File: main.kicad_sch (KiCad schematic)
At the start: 30 parts, among them J1 USB_C_Receptacle_USB2.0_16P, J2 Conn_ARM_JTAG_SWD_10, U1 XC6206PxxxMR, U2 USBLC6-2SC6, U3 CH340N, U4 E73-2G4M04S1B

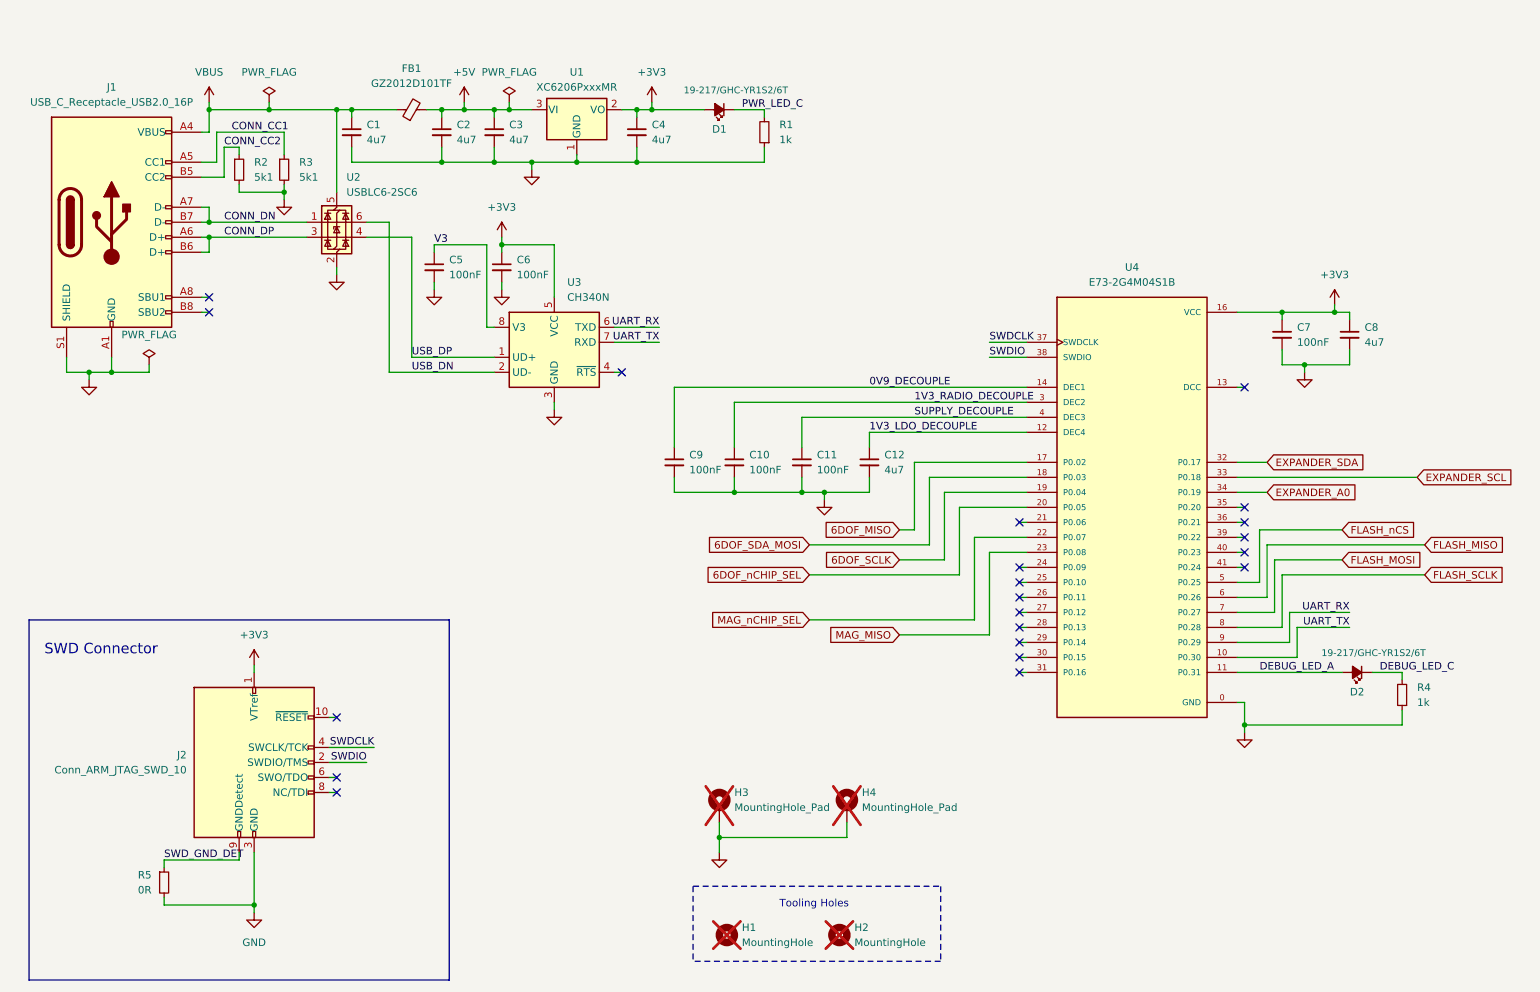
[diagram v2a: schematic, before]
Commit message: Cleaned up schematic with comments from datasheets.  Added stitching vias to PCB
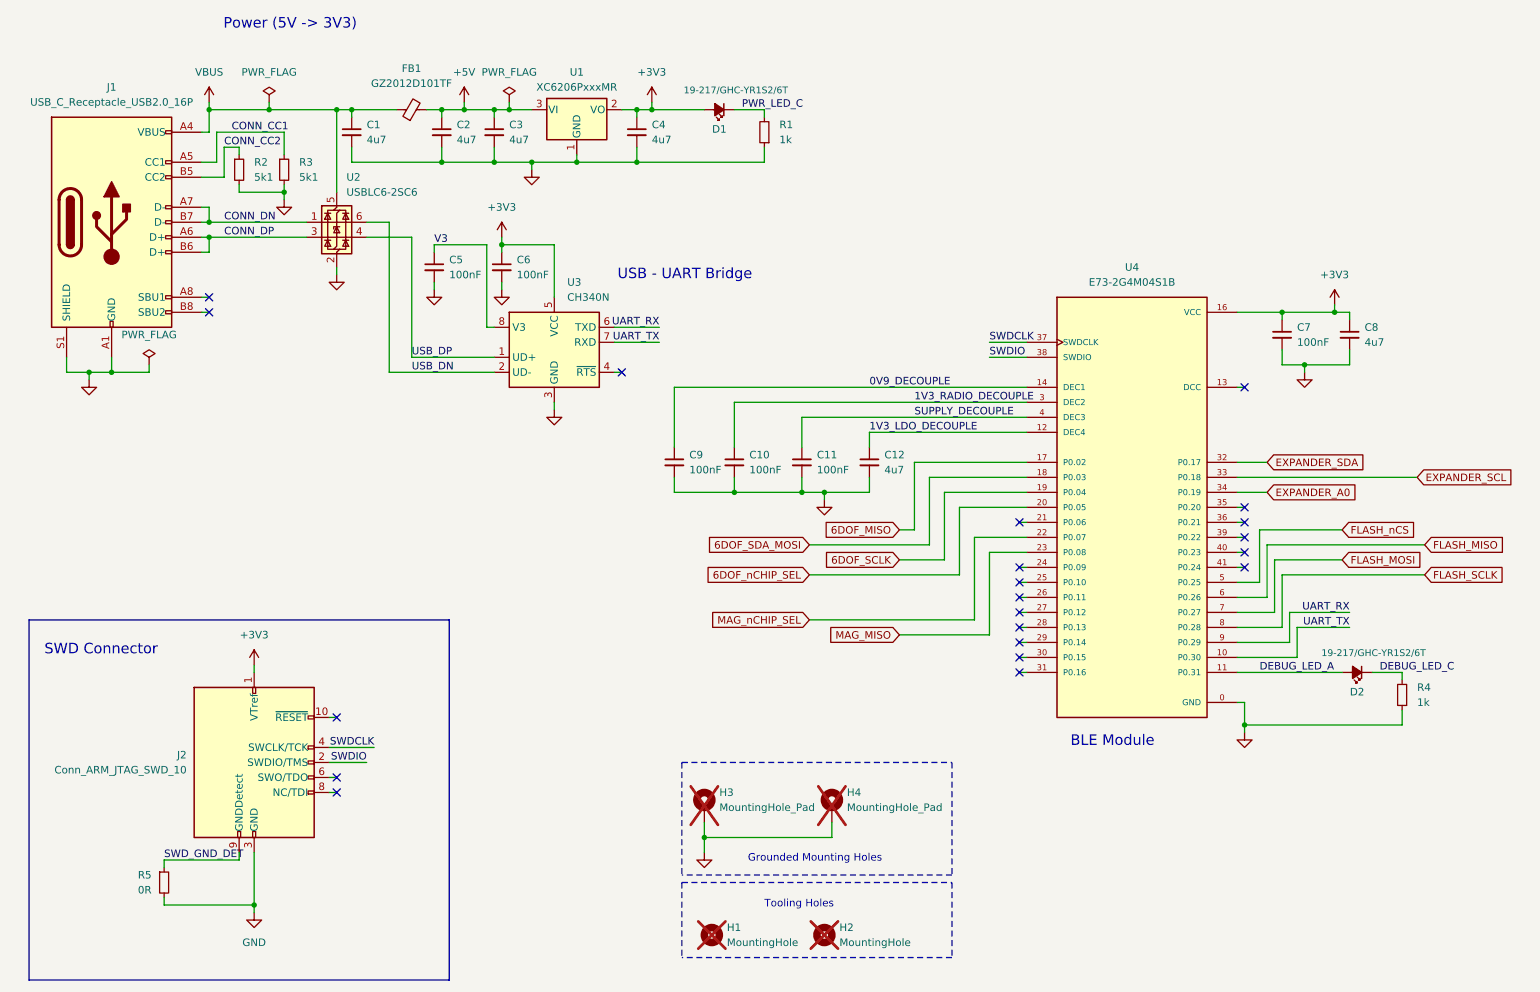
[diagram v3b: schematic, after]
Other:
- note added: "BLE Module"
- note added: "Grounded Mounting Holes"
- note added: "Power (5V -> 3V3)"
- note added: "USB - UART Bridge"
- moved on the sheet: H1, H2, H3, H4
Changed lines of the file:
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@@
 	)
 	(junction
-		(at 133.35 168.91)
+		(at 130.81 168.91)
 		(diameter 0)
 		(color 0 0 0 0)
@@
 		)
 	)
+	(polyline
+		(pts
+			(xy 127 156.21) (xy 127 175.26)
+		)
+		(stroke
+			(width 0)
+			(type dash)
+		)
+	)
 	(wire
 		(pts
@@
 		)
 	)
+	(polyline
+		(pts
+			(xy 172.72 175.26) (xy 127 175.26)
+		)
+		(stroke
+			(width 0)
+			(type dash)
+		)
+	)
 	(wire
 		(pts
@@
 		)
 	)
+	(polyline
+		(pts
+			(xy 127 156.21) (xy 172.72 156.21)
+		)
+		(stroke
+			(width 0)
+			(type dash)
+		)
+	)
 	(wire
 		(pts
@@
 	(polyline
 		(pts
-			(xy 170.815 177.165) (xy 170.815 189.865)
+			(xy 172.72 176.53) (xy 172.72 189.23)
 		)
 		(stroke
@@
 	(wire
 		(pts
-			(xy 133.35 168.91) (xy 133.35 171.45)
+			(xy 130.81 168.91) (xy 130.81 171.45)
 		)
 		(stroke
@@
 	(polyline
 		(pts
-			(xy 128.905 177.165) (xy 128.905 189.865)
+			(xy 127 176.53) (xy 127 189.23)
 		)
 		(stroke
@@
 	(polyline
 		(pts
-			(xy 170.815 189.865) (xy 128.905 189.865)
+			(xy 172.72 189.23) (xy 127 189.23)
 		)
 		(stroke
@@
 	(wire
 		(pts
-			(xy 133.35 166.37) (xy 133.35 168.91)
+			(xy 130.81 166.37) (xy 130.81 168.91)
 		)
 		(stroke
@@
 	(wire
 		(pts
-			(xy 133.35 168.91) (xy 154.94 168.91)
+			(xy 130.81 168.91) (xy 152.4 168.91)
 		)
 		(stroke
@@
 	(polyline
 		(pts
-			(xy 128.905 177.165) (xy 170.815 177.165)
+			(xy 127 176.53) (xy 172.72 176.53)
 		)
 		(stroke
@@
 		)
 	)
+	(polyline
+		(pts
+			(xy 172.72 156.21) (xy 172.72 175.26)
+		)
+		(stroke
+			(width 0)
+			(type dash)
+		)
+	)
 	(wire
 		(pts
@@
 	(wire
 		(pts
-			(xy 154.94 166.37) (xy 154.94 168.91)
+			(xy 152.4 166.37) (xy 152.4 168.91)
 		)
 		(stroke
@@
 		)
 	)
+	(text "USB - UART Bridge"
+		(exclude_from_sim no)
+		(at 127.508 73.66 0)
+		(effects
+			(font
+				(size 1.778 1.778)
+			)
+		)
+	)
+	(text "Grounded Mounting Holes"
+		(exclude_from_sim no)
+		(at 138.176 173.228 0)
+		(effects
+			(font
+				(size 1.27 1.27)
+			)
+			(justify left bottom)
+		)
+	)
 	(text "Tooling Holes"
 		(exclude_from_sim no)
-		(at 143.51 180.975 0)
+		(at 140.97 180.975 0)
 		(effects
 			(font
@@
 		)
 	)
+	(text "Power (5V -> 3V3)"
+		(exclude_from_sim no)
+		(at 60.706 31.242 0)
+		(effects
+			(font
+				(size 1.778 1.778)
+			)
+		)
+	)
+	(text "BLE Module"
+		(exclude_from_sim no)
+		(at 199.898 152.654 0)
+		(effects
+			(font
+				(size 1.778 1.778)
+			)
+		)
+	)
 	(text "SWD Connector"
 		(exclude_from_sim no)
@@
 	(symbol
 		(lib_id "Mechanical:MountingHole_Pad")
-		(at 154.94 163.83 0)
+		(at 152.4 163.83 0)
 		(unit 1)
 		(exclude_from_sim no)
@@
 		(fields_autoplaced yes)
 		(property "Reference" "H4"
-			(at 157.48 161.2899 0)
+			(at 154.94 161.2899 0)
 			(effects
 				(font
@@
 		)
 		(property "Value" "MountingHole_Pad"
-			(at 157.48 163.8299 0)
+			(at 154.94 163.8299 0)
 			(effects
 				(font
@@
 		)
 		(property "Footprint" "MountingHole:MountingHole_2.2mm_M2_Pad"
-			(at 154.94 163.83 0)
+			(at 152.4 163.83 0)
 			(effects
 				(font
@@
 		)
 		(property "Datasheet" "~"
-			(at 154.94 163.83 0)
+			(at 152.4 163.83 0)
 			(effects
 				(font
@@
 		)
 		(property "Description" "Mounting Hole with connection"
-			(at 154.94 163.83 0)
+			(at 152.4 163.83 0)
 			(effects
 				(font
@@
 	(symbol
 		(lib_id "Mechanical:MountingHole_Pad")
-		(at 133.35 163.83 0)
+		(at 130.81 163.83 0)
 		(unit 1)
 		(exclude_from_sim no)
@@
 		(fields_autoplaced yes)
 		(property "Reference" "H3"
-			(at 135.89 161.2899 0)
+			(at 133.35 161.2899 0)
 			(effects
 				(font
@@
 		)
 		(property "Value" "MountingHole_Pad"
-			(at 135.89 163.8299 0)
+			(at 133.35 163.8299 0)
 			(effects
 				(font
@@
 		)
 		(property "Footprint" "MountingHole:MountingHole_2.2mm_M2_Pad"
-			(at 133.35 163.83 0)
+			(at 130.81 163.83 0)
 			(effects
 				(font
@@
 		)
 		(property "Datasheet" "~"
-			(at 133.35 163.83 0)
+			(at 130.81 163.83 0)
 			(effects
 				(font
@@
 		)
 		(property "Description" "Mounting Hole with connection"
-			(at 133.35 163.83 0)
+			(at 130.81 163.83 0)
 			(effects
 				(font
@@
 	(symbol
 		(lib_id "Mechanical:MountingHole")
-		(at 153.67 185.42 0)
+		(at 151.13 185.42 0)
 		(unit 1)
 		(exclude_from_sim no)
@@
 		(fields_autoplaced yes)
 		(property "Reference" "H2"
-			(at 156.21 184.1499 0)
+			(at 153.67 184.1499 0)
 			(effects
 				(font
@@
 		)
 		(property "Value" "MountingHole"
-			(at 156.21 186.6899 0)
+			(at 153.67 186.6899 0)
 			(effects
 				(font
@@
 		)
 		(property "Footprint" "JLCPCB:JLCPCB_ToolingHole_45.4mils"
-			(at 153.67 185.42 0)
+			(at 151.13 185.42 0)
 			(effects
 				(font
@@
 		)
 		(property "Datasheet" "~"
-			(at 153.67 185.42 0)
+			(at 151.13 185.42 0)
 			(effects
 				(font
@@
 		)
 		(property "Description" ""
-			(at 153.67 185.42 0)
+			(at 151.13 185.42 0)
 			(effects
 				(font
@@
 		(lib_name "GND_1")
 		(lib_id "power:GND")
-		(at 133.35 171.45 0)
+		(at 130.81 171.45 0)
 		(unit 1)
 		(exclude_from_sim no)
@@
 		(fields_autoplaced yes)
 		(property "Reference" "#PWR028"
-			(at 133.35 177.8 0)
+			(at 130.81 177.8 0)
 			(effects
 				(font
@@
 		)
 		(property "Value" "GND"
-			(at 133.35 176.53 0)
+			(at 130.81 176.53 0)
 			(effects
 				(font
@@
 		)
 		(property "Footprint" ""
-			(at 133.35 171.45 0)
+			(at 130.81 171.45 0)
 			(effects
 				(font
@@
 		)
 		(property "Datasheet" ""
-			(at 133.35 171.45 0)
+			(at 130.81 171.45 0)
 			(effects
 				(font
@@
 		)
 		(property "Description" "Power symbol creates a global label with name \"GND\" , ground"
-			(at 133.35 171.45 0)
+			(at 130.81 171.45 0)
 			(effects
 				(font
@@
 	(symbol
 		(lib_id "Mechanical:MountingHole")
-		(at 134.62 185.42 0)
+		(at 132.08 185.42 0)
 		(unit 1)
 		(exclude_from_sim no)
@@
 		(fields_autoplaced yes)
 		(property "Reference" "H1"
-			(at 137.16 184.1499 0)
+			(at 134.62 184.1499 0)
 			(effects
 				(font
@@
 		)
 		(property "Value" "MountingHole"
-			(at 137.16 186.6899 0)
+			(at 134.62 186.6899 0)
 			(effects
 				(font
@@
 		)
 		(property "Footprint" "JLCPCB:JLCPCB_ToolingHole_45.4mils"
-			(at 134.62 185.42 0)
+			(at 132.08 185.42 0)
 			(effects
 				(font
@@
 		)
 		(property "Datasheet" "~"
-			(at 134.62 185.42 0)
+			(at 132.08 185.42 0)
 			(effects
 				(font
@@
 		)
 		(property "Description" ""
-			(at 134.62 185.42 0)
+			(at 132.08 185.42 0)
 			(effects
 				(font

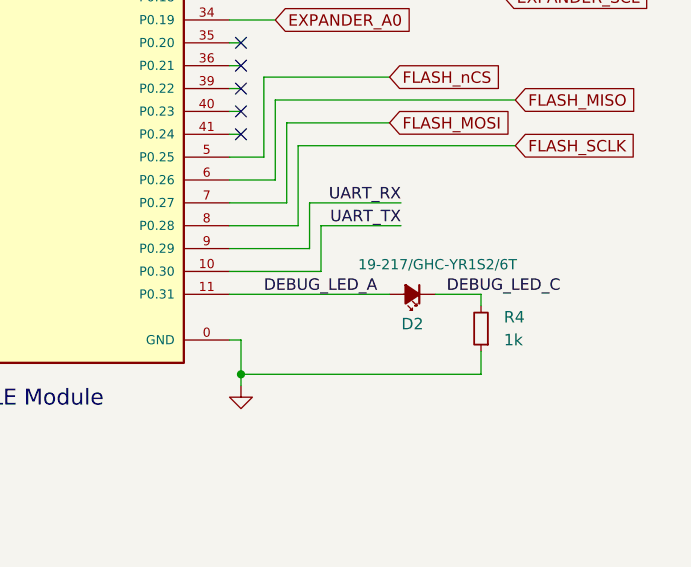
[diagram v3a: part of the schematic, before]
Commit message: Switched around debug LED pinout with a UART line to be compatible with a previous design
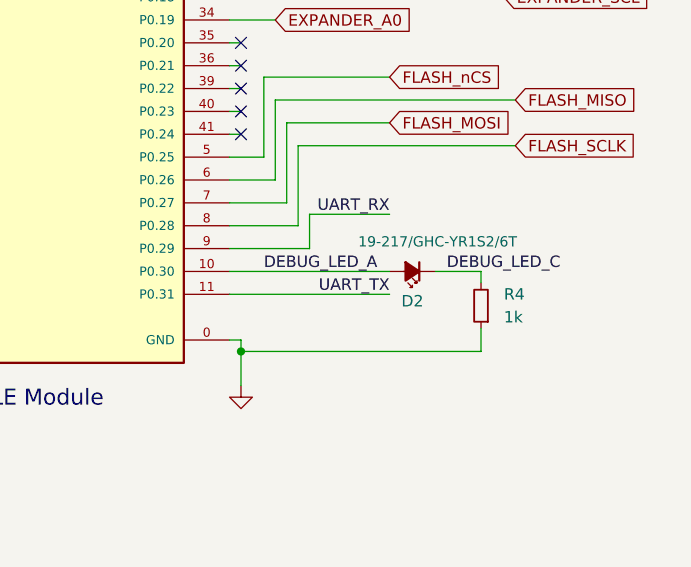
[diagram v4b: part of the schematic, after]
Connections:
- net DEBUG_LED_A: now also U4.10 (P0.30); no longer U4.11 (P0.31)
- net UART_TX: now also U4.11 (P0.31); no longer U4.10 (P0.30)
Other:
- moved on the sheet: D2, R4
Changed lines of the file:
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@@
 	)
 	(junction
-		(at 222.25 149.86)
-		(diameter 0)
-		(color 0 0 0 0)
-	)
-	(junction
 		(at 95.25 45.72)
 		(diameter 0)
@@
 	)
 	(junction
+		(at 222.25 147.32)
+		(diameter 0)
+		(color 0 0 0 0)
+	)
+	(junction
 		(at 30.48 90.17)
 		(diameter 0)
@@
 	(wire
 		(pts
-			(xy 222.25 149.86) (xy 222.25 151.13)
-		)
-		(stroke
-			(width 0)
-			(type default)
-		)
-	)
-	(wire
-		(pts
 			(xy 184.15 138.43) (xy 185.42 138.43)
 		)
@@
 	(wire
 		(pts
-			(xy 222.25 146.05) (xy 222.25 149.86)
+			(xy 222.25 146.05) (xy 222.25 147.32)
 		)
 		(stroke
@@
 	(wire
 		(pts
-			(xy 229.87 130.81) (xy 229.87 135.89)
+			(xy 229.87 132.08) (xy 229.87 135.89)
 		)
 		(stroke
@@
 	(wire
 		(pts
+			(xy 222.25 147.32) (xy 222.25 151.13)
+		)
+		(stroke
+			(width 0)
+			(type default)
+		)
+	)
+	(wire
+		(pts
 			(xy 130.81 168.91) (xy 130.81 171.45)
 		)
@@
 	(wire
 		(pts
-			(xy 231.14 138.43) (xy 231.14 133.35)
-		)
-		(stroke
-			(width 0)
-			(type default)
-		)
-	)
-	(wire
-		(pts
 			(xy 85.09 68.58) (xy 85.09 69.85)
 		)
@@
 	(wire
 		(pts
-			(xy 220.98 138.43) (xy 231.14 138.43)
-		)
-		(stroke
-			(width 0)
-			(type default)
-		)
-	)
-	(wire
-		(pts
 			(xy 81.28 67.31) (xy 73.66 67.31)
 		)
@@
 	(wire
 		(pts
-			(xy 231.14 133.35) (xy 240.03 133.35)
-		)
-		(stroke
-			(width 0)
-			(type default)
-		)
-	)
-	(wire
-		(pts
-			(xy 248.92 142.24) (xy 248.92 140.97)
+			(xy 248.92 139.7) (xy 248.92 138.43)
 		)
 		(stroke
@@
 	(wire
 		(pts
-			(xy 222.25 149.86) (xy 248.92 149.86)
+			(xy 222.25 147.32) (xy 248.92 147.32)
 		)
 		(stroke
@@
 	(wire
 		(pts
-			(xy 248.92 147.32) (xy 248.92 149.86)
+			(xy 248.92 144.78) (xy 248.92 147.32)
 		)
 		(stroke
@@
 	(wire
 		(pts
-			(xy 240.03 130.81) (xy 229.87 130.81)
+			(xy 238.76 132.08) (xy 229.87 132.08)
 		)
 		(stroke
@@
 	(wire
 		(pts
-			(xy 248.92 140.97) (xy 243.84 140.97)
+			(xy 248.92 138.43) (xy 243.84 138.43)
 		)
 		(stroke
@@
 	(wire
 		(pts
+			(xy 220.98 138.43) (xy 238.76 138.43)
+		)
+		(stroke
+			(width 0)
+			(type default)
+		)
+	)
+	(wire
+		(pts
 			(xy 67.31 158.75) (xy 68.58 158.75)
 		)
@@
 	(wire
 		(pts
-			(xy 220.98 107.95) (xy 251.46 107.95)
+			(xy 220.98 140.97) (xy 238.76 140.97)
 		)
 		(stroke
@@
 	(wire
 		(pts
-			(xy 59.69 49.53) (xy 48.26 49.53)
+			(xy 220.98 107.95) (xy 251.46 107.95)
 		)
 		(stroke
@@
 	(wire
 		(pts
-			(xy 184.15 133.35) (xy 185.42 133.35)
+			(xy 59.69 49.53) (xy 48.26 49.53)
 		)
 		(stroke
@@
 	(wire
 		(pts
-			(xy 232.41 88.9) (xy 240.03 88.9)
+			(xy 184.15 133.35) (xy 185.42 133.35)
 		)
 		(stroke
@@
 	(wire
 		(pts
-			(xy 176.53 118.11) (xy 185.42 118.11)
+			(xy 232.41 88.9) (xy 240.03 88.9)
 		)
 		(stroke
@@
 	(wire
 		(pts
-			(xy 81.28 87.63) (xy 81.28 67.31)
+			(xy 176.53 118.11) (xy 185.42 118.11)
 		)
 		(stroke
@@
 	(wire
 		(pts
-			(xy 220.98 140.97) (xy 238.76 140.97)
+			(xy 81.28 87.63) (xy 81.28 67.31)
 		)
 		(stroke
@@
 	)
 	(label "DEBUG_LED_C"
-		(at 245.11 140.97 0)
+		(at 245.11 138.43 0)
 		(fields_autoplaced yes)
 		(effects
@@
 		)
 	)
-	(label "UART_TX"
-		(at 240.03 133.35 180)
-		(fields_autoplaced yes)
-		(effects
-			(font
-				(size 1.27 1.27)
-			)
-			(justify right bottom)
-		)
-	)
 	(label "SWDIO"
 		(at 73.66 156.21 180)
@@
 	)
 	(label "DEBUG_LED_A"
-		(at 224.79 140.97 0)
+		(at 224.79 138.43 0)
 		(fields_autoplaced yes)
 		(effects
@@
 	)
 	(label "UART_RX"
-		(at 240.03 130.81 180)
+		(at 238.76 132.08 180)
 		(fields_autoplaced yes)
 		(effects
@@
 	)
 	(label "UART_TX"
+		(at 238.76 140.97 180)
+		(fields_autoplaced yes)
+		(effects
+			(font
+				(size 1.27 1.27)
+			)
+			(justify right bottom)
+		)
+	)
+	(label "UART_TX"
 		(at 123.19 85.09 180)
 		(fields_autoplaced yes)
@@
 	(symbol
 		(lib_id "Device:LED_Small_Filled")
-		(at 241.3 140.97 180)
+		(at 241.3 138.43 180)
 		(unit 1)
 		(exclude_from_sim no)
@@
 		(dnp no)
 		(property "Reference" "D2"
-			(at 241.3 144.272 0)
+			(at 241.3 141.732 0)
 			(effects
 				(font
@@
 		)
 		(property "Value" "19-217/GHC-YR1S2/6T"
-			(at 244.094 137.668 0)
+			(at 244.094 135.128 0)
 			(effects
 				(font
@@
 		)
 		(property "Footprint" "LED_SMD:LED_0603_1608Metric"
-			(at 241.3 140.97 90)
+			(at 241.3 138.43 90)
 			(effects
 				(font
@@
 		)
 		(property "Datasheet" "https://datasheet.lcsc.com/lcsc/2207051802_Everlight-Elec-19-217-GHC-YR1S2-6T_C2986059.pdf"
-			(at 241.3 140.97 90)
+			(at 241.3 138.43 90)
 			(effects
 				(font
@@
 		)
 		(property "Description" ""
-			(at 241.3 140.97 0)
+			(at 241.3 138.43 0)
 			(effects
 				(font
@@
 		)
 		(property "LCSC Part #" "C2986059"
-			(at 241.3 140.97 0)
+			(at 241.3 138.43 0)
 			(effects
 				(font
@@
 		)
 		(property "Manufacturer" "Everlight Electronics Co Ltd"
-			(at 241.3 140.97 0)
+			(at 241.3 138.43 0)
 			(effects
 				(font
@@
 		)
 		(property "Manufacturer Part Number" "19-217/GHC-YR1S2/6T"
-			(at 241.3 140.97 0)
+			(at 241.3 138.43 0)
 			(effects
 				(font
@@
 	(symbol
 		(lib_id "Device:R_Small")
-		(at 248.92 144.78 180)
+		(at 248.92 142.24 180)
 		(unit 1)
 		(exclude_from_sim no)
@@
 		(fields_autoplaced yes)
 		(property "Reference" "R4"
-			(at 251.46 143.5099 0)
+			(at 251.46 140.9699 0)
 			(effects
 				(font
@@
 		)
 		(property "Value" "1k"
-			(at 251.46 146.0499 0)
+			(at 251.46 143.5099 0)
 			(effects
 				(font
@@
 		)
 		(property "Footprint" "Resistor_SMD:R_0603_1608Metric"
-			(at 248.92 144.78 0)
+			(at 248.92 142.24 0)
 			(effects
 				(font
@@
 		)
 		(property "Datasheet" "https://datasheet.lcsc.com/lcsc/2206010130_UNI-ROYAL-Uniroyal-Elec-0603WAF1001T5E_C21190.pdf"
-			(at 248.92 144.78 0)
+			(at 248.92 142.24 0)
 			(effects
 				(font
@@
 		)
 		(property "Description" "Resistor, small symbol"
-			(at 248.92 144.78 0)
+			(at 248.92 142.24 0)
 			(effects
 				(font
@@
 		)
 		(property "Manufacturer" "UNI-ROYAL"
-			(at 248.92 144.78 0)
+			(at 248.92 142.24 0)
 			(effects
 				(font
@@
 		)
 		(property "Manufacturer Part Number" "0603WAF1001T5E"
-			(at 248.92 144.78 0)
+			(at 248.92 142.24 0)
 			(effects
 				(font
@@
 		)
 		(property "LCSC Part #" "C21190"
-			(at 248.92 144.78 0)
+			(at 248.92 142.24 0)
 			(effects
 				(font
